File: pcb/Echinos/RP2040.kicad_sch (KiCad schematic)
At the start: 29 parts, among them J9 TagConnect_6pins, SW2 SW_Push, SW3 SW_Push, U4 W25Q128JVS, U5 RP2040, U6 74LVC1T45, X1 CMOS -12MHz

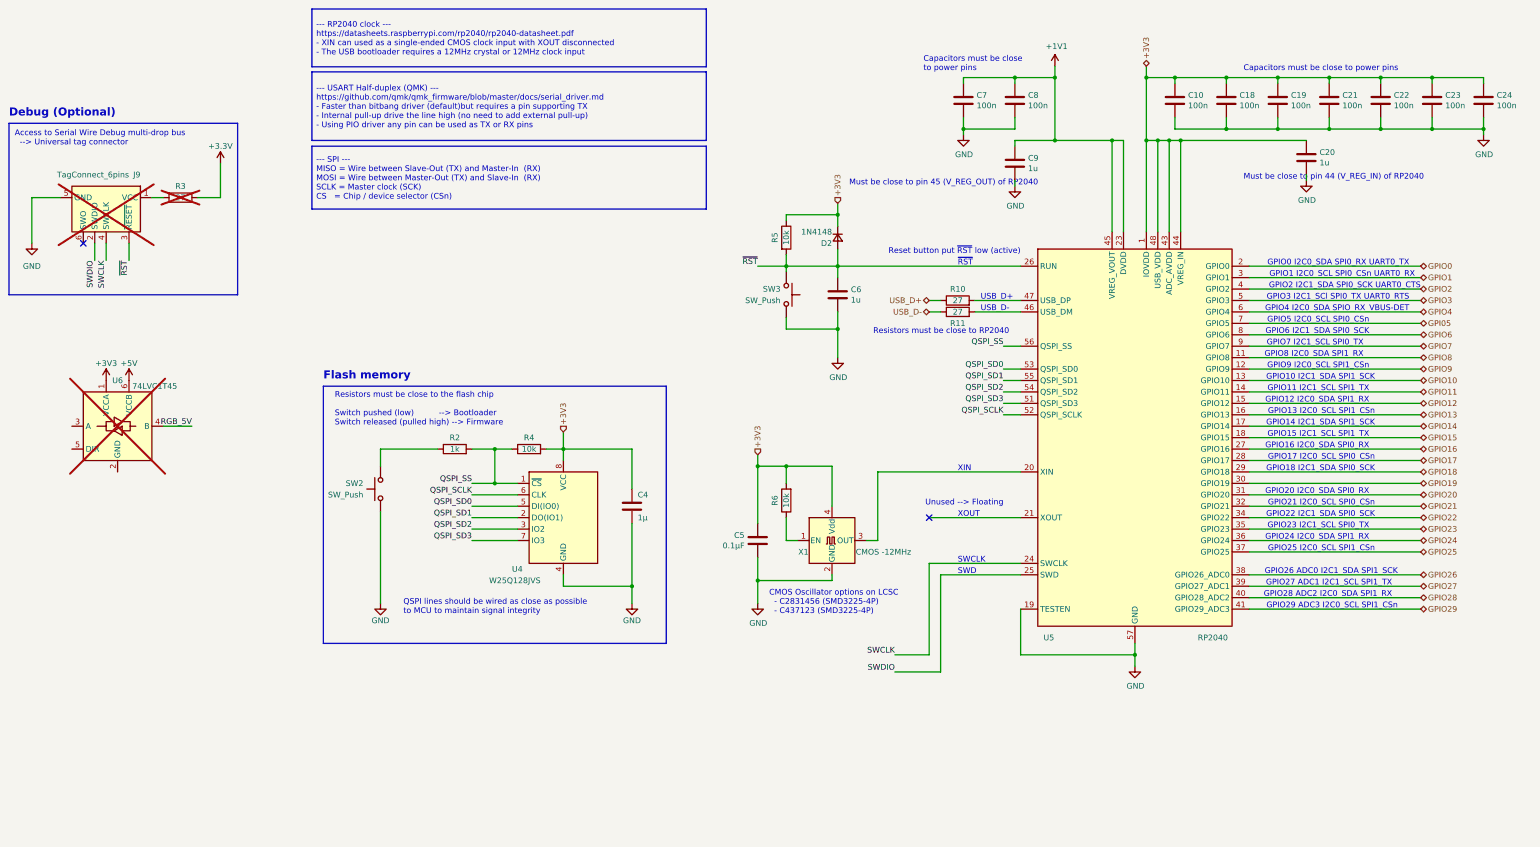
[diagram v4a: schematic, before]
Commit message: [PCB] - Save last state with on board RP2040.
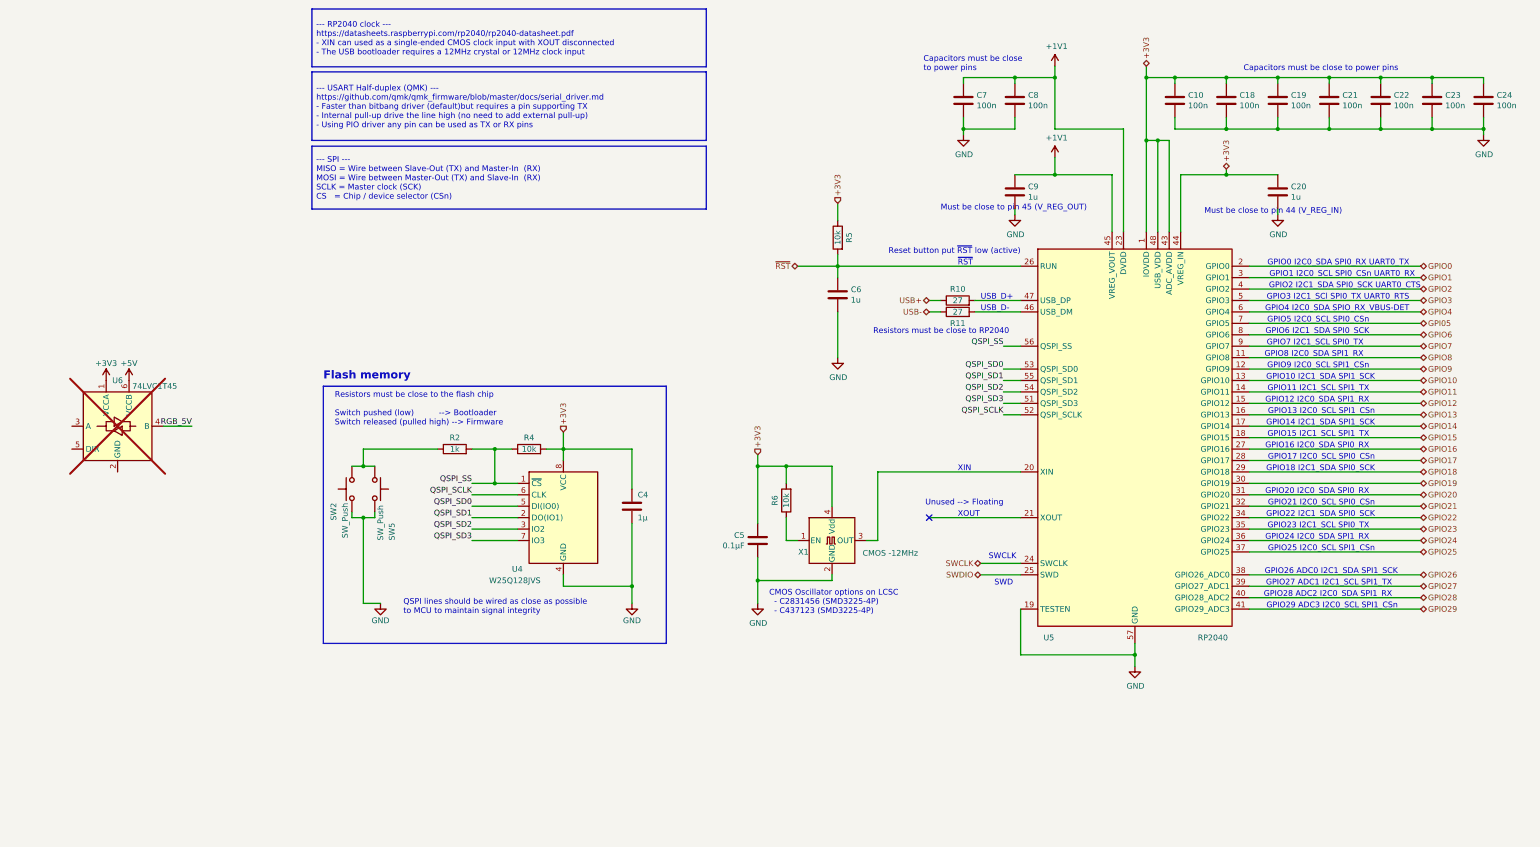
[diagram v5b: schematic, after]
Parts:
- removed D2: 1N4148, Diode_SMD:D_SOD-323_HandSoldering, symbol Device:D_Small
- removed J9: TagConnect_6pins, Connector:Tag-Connect_TC2030-IDC-FP_2x03_P1.27mm_Vertical, symbol Connector:Conn_ARM_SWD_TagConnect_TC2030
- removed R3: 27, Resistor_SMD:R_0402_1005Metric_Pad0.72x0.64mm_HandSolder, symbol Device:R
- removed SW3: SW_Push, Button_Switch_SMD:SW_SPST_CK_KXT3, symbol Switch:SW_Push
- added SW5: SW_Push, Button_Switch_SMD:SW_SPST_TS-1088-xR020, symbol Switch:SW_Push
- SW2: footprint Button_Switch_SMD:SW_SPST_CK_KXT3 -> Button_Switch_SMD:SW_SPST_TS-1088-xR020
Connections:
- net GND: now also SW5.2
- net at R2.1, SW2.2: now also SW5.1
- net USB_D+ renamed USB+
- net USB_D- renamed USB-
- no-connect marks 2 -> 1
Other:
- note added: "Must be close to pin 44 (V_REG_IN)"
- note added: "Must be close to pin 45 (V_REG_OUT)"
- note removed: "Access to Serial Wire Debug multi-drop bus --> Universal tag connector"
- note removed: "Debug (Optional)"
- note removed: "Must be close to pin 44 (V_REG_IN) of RP2040"
- note removed: "Must be close to pin 45 (V_REG_OUT) of RP2040"
- moved on the sheet: C20, C9, R5, SW2

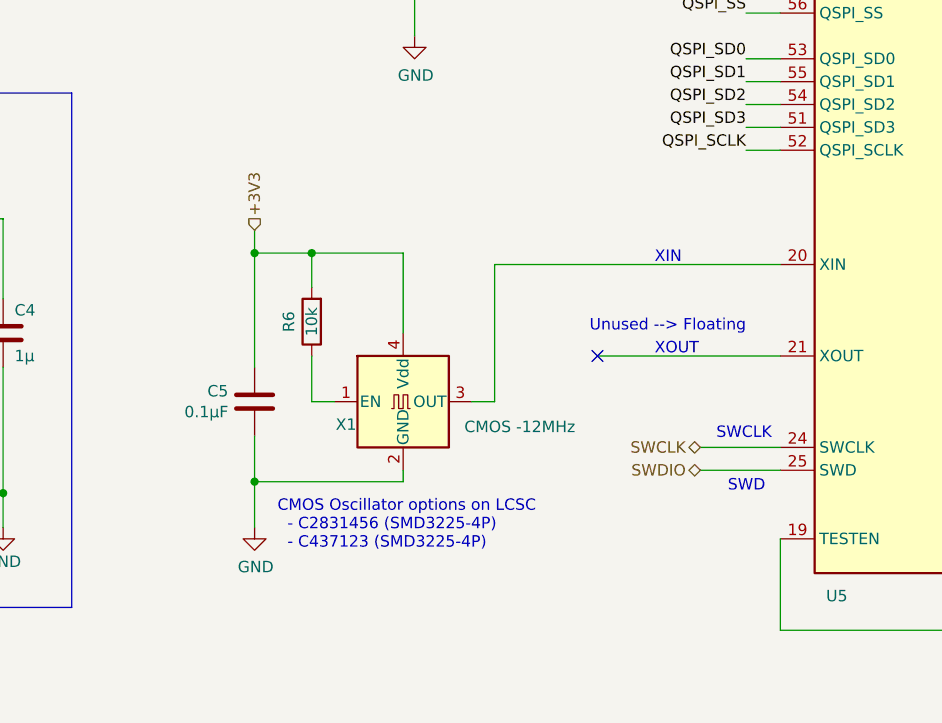
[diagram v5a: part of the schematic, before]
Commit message: [PCB] - Save last state with on board RP2040.   - Route crystal and 1V1
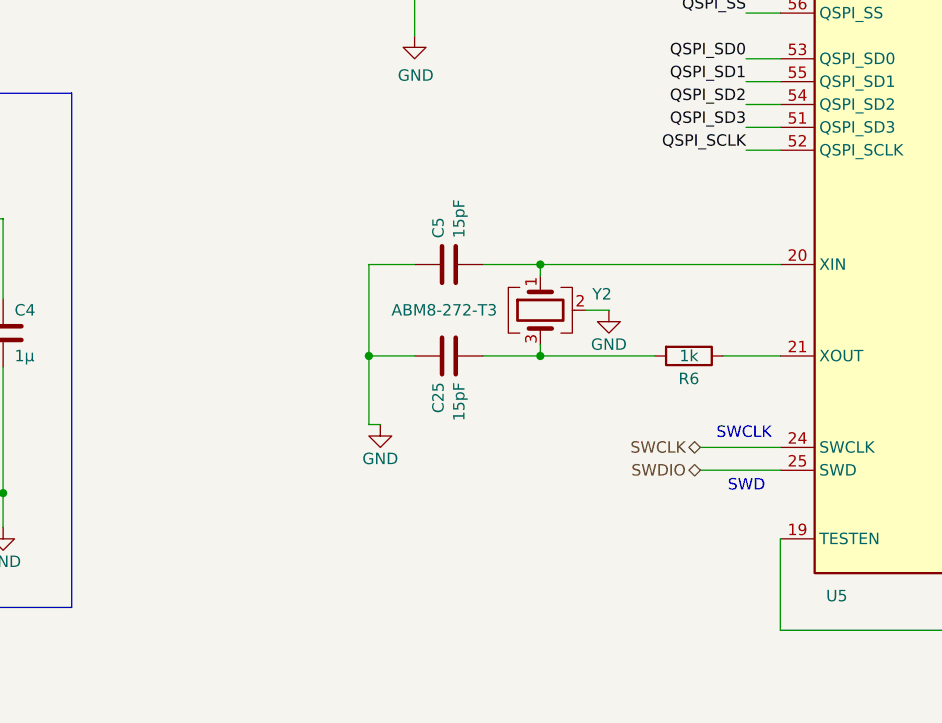
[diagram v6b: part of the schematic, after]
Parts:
- removed X1: CMOS -12MHz, Oscillator:Oscillator_SMD_Abracon_ASE-4Pin_3.2x2.5mm_HandSoldering, symbol Oscillator:ASE-xxxMHz
- added C25: 15pF, Capacitor_SMD:C_0402_1005Metric_Pad0.74x0.62mm_HandSolder, symbol Device:C
- added Y2: Crystal_GND24, Crystal:Crystal_SMD_Abracon_ABM8G-4Pin_3.2x2.5mm, symbol Device:Crystal_GND24
- C5: value 0.1µF -> 15pF; LCSC C5139511 -> C86285
- R6: value 10k -> 1k; LCSC C25744 -> C11702
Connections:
- net +3V3: no longer C5.1, R6.2
- net GND: now also C5.1, C25.1, Y2.2 (G), Y2.4 (G); no longer C5.2
- net at R6.1: now also U5.21 (XOUT)
- net at U5.20 (XIN): now also C5.2, Y2.1
- new net: C25.2, R6.2, Y2.3
- no-connect marks 1 -> 0
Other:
- note removed: "CMOS Oscillator options on LCSC - C2831456 (SMD3225-4P) - C437123 (SMD3225-4P)"
- note removed: "Unused --> Floating"
- note removed: "XIN"
- note removed: "XOUT"
- moved on the sheet: C5, R6

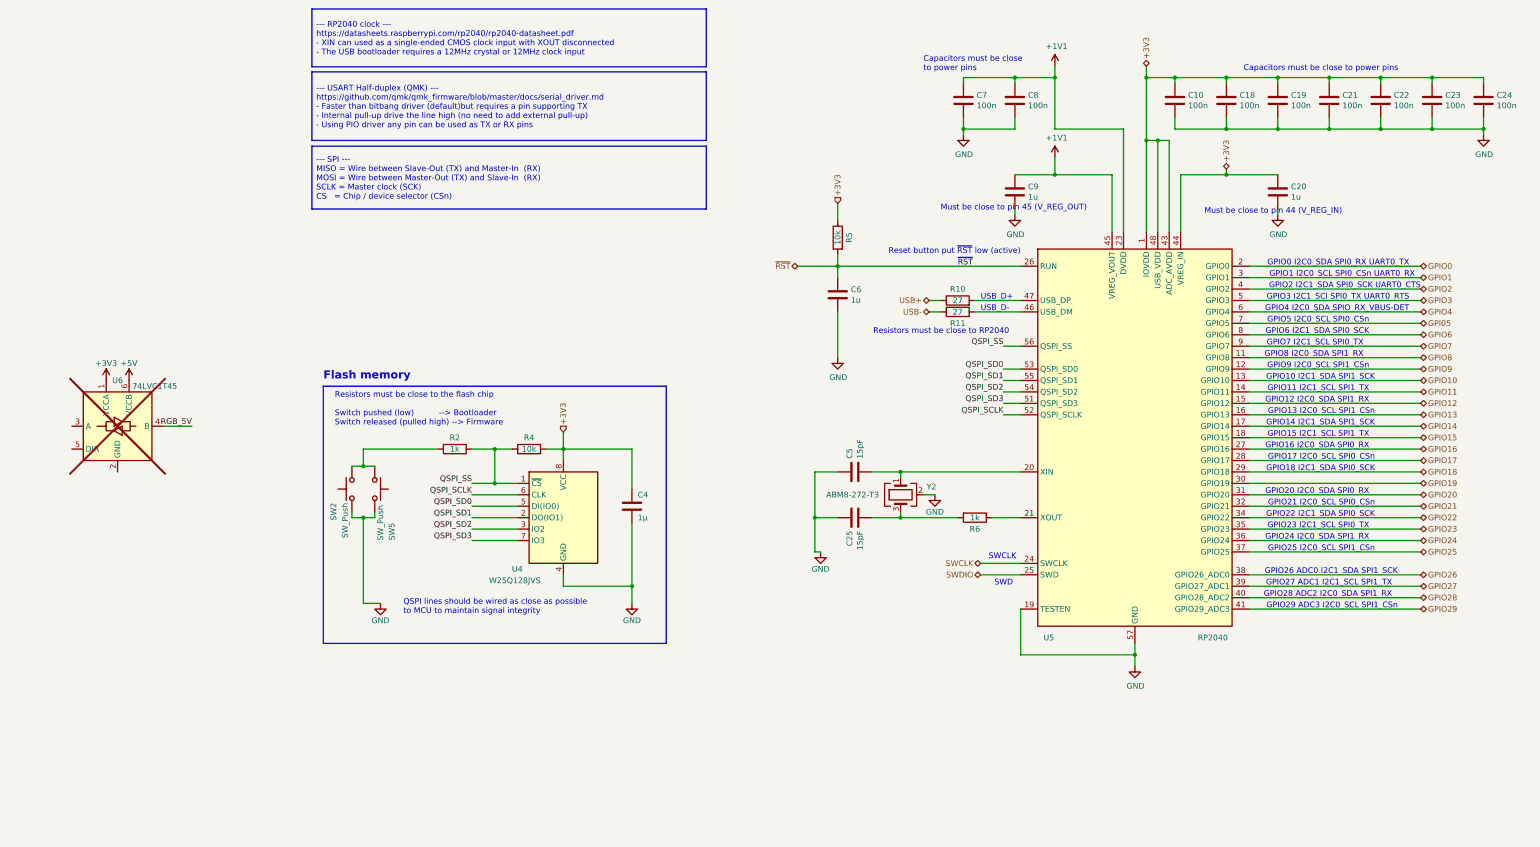
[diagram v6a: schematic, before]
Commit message: [PCB] - Save last state with on board RP2040.   - Clean schematics   - Fix flash capacitor value   - Fix flash schema to match all footprint pins   - Pass ERC (schema and pcb)   - Select missing LCSC components (USBC/B, buttons, vik connector)   - Add more margin to lateral pads in USB B footprint   - Improve top plane grounding under switches   - Adjust orientation and position to match JLCPCB   - Clean unused fields in schematics   - Add VIK connector footprint to lib (updated to match more models)   - Harmonization of footprints packaging for caps and resistors (either 0805 or 0402)   - Check availability and correctness of all parts   - Fix space in fields (was LCSC2 on leds)
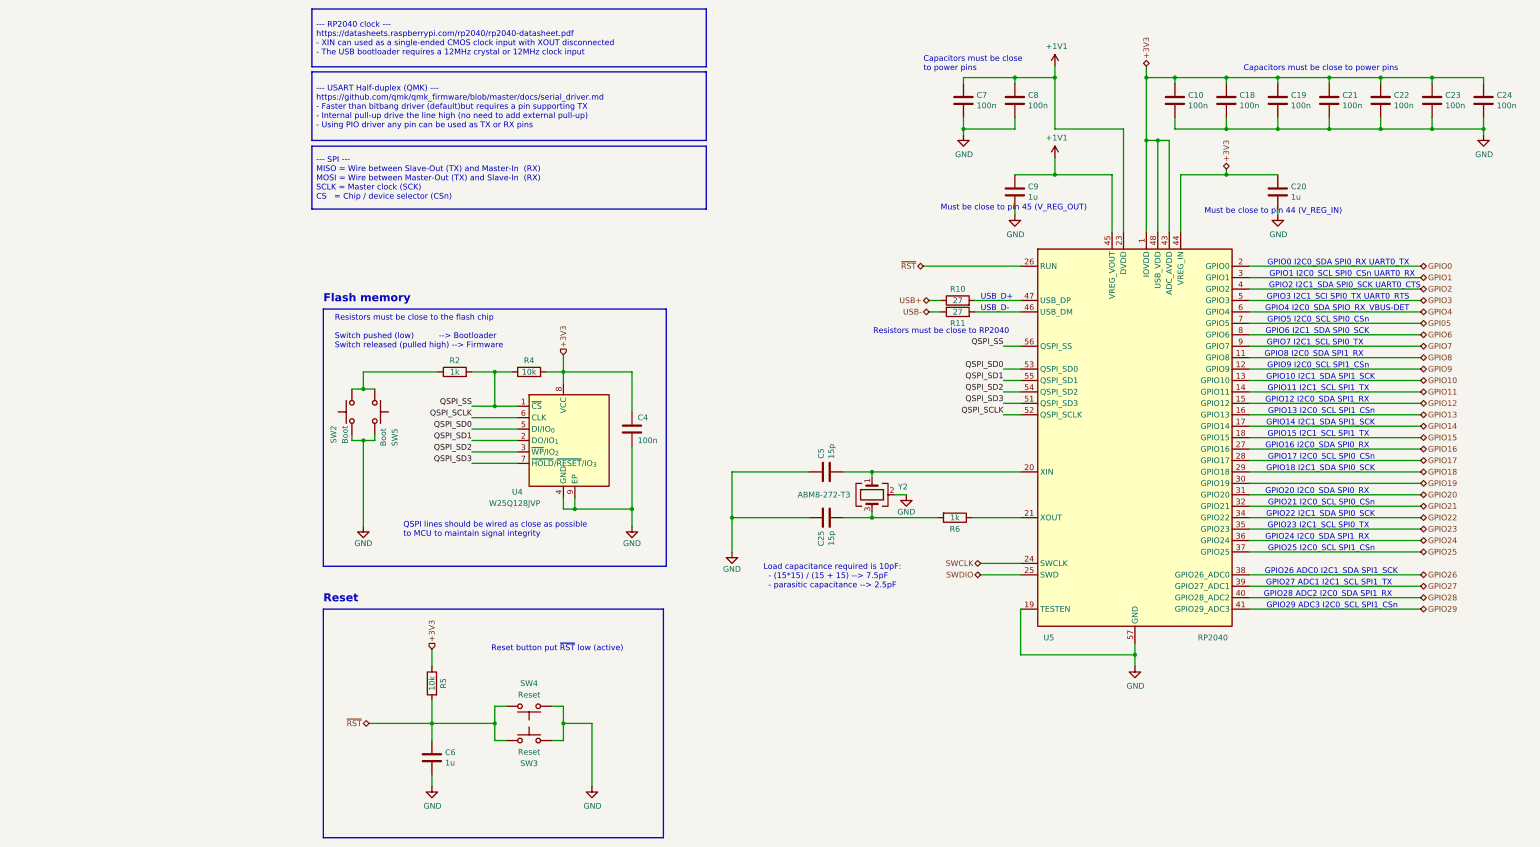
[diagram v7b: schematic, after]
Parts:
- removed U6: 74LVC1T45, Package_TO_SOT_SMD:SOT-563, symbol Logic_LevelTranslator:SN74LVC1T45DRL
- added SW3, SW4: Reset, Button_Switch_SMD:SW_SPST_TS-1088-xR020, symbol Switch:SW_Push
- C20, C9: LCSC C458913 -> C14445
- C25, C5: value 15pF -> 15p
- C4: value 1µ -> 100n; footprint Capacitor_SMD:C_0603_1608Metric_Pad1.08x0.95mm_HandSolder -> Capacitor_SMD:C_0805_2012Metric; LCSC C19666 -> C1711
- C6: LCSC C19666 -> C14445
- SW2, SW5: value SW_Push -> Boot; LCSC C319433 -> C720477
- U4: value W25Q128JVS -> W25Q128JVP; symbol Memory_Flash:W25Q128JVS -> Memory_Flash:W25Q128JVP; MPN (none) -> W25Q128JVPIQ
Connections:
- net GND: now also U4.9 (EP), SW3.2, SW4.1
- net ~{RST}: now also SW3.1, SW4.2
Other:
- note added: "Load capacitance required is 10pF: - (15*15) / (15 + 15) --> 7.5pF - parasitic capacitance --> 2.5pF"
- note added: "Reset"
- note removed: "SWCLK"
- note removed: "SWD"
- note removed: "~{RST}"
- moved on the sheet: C25, C4, C5, C6, R2, R4, R5, R6, SW2, SW5, Y2

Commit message: [PCB] - Save last state with on board RP2040.   - Create right side and route all components   - Component still on the bottom side to be able to merge both side for manufacturing
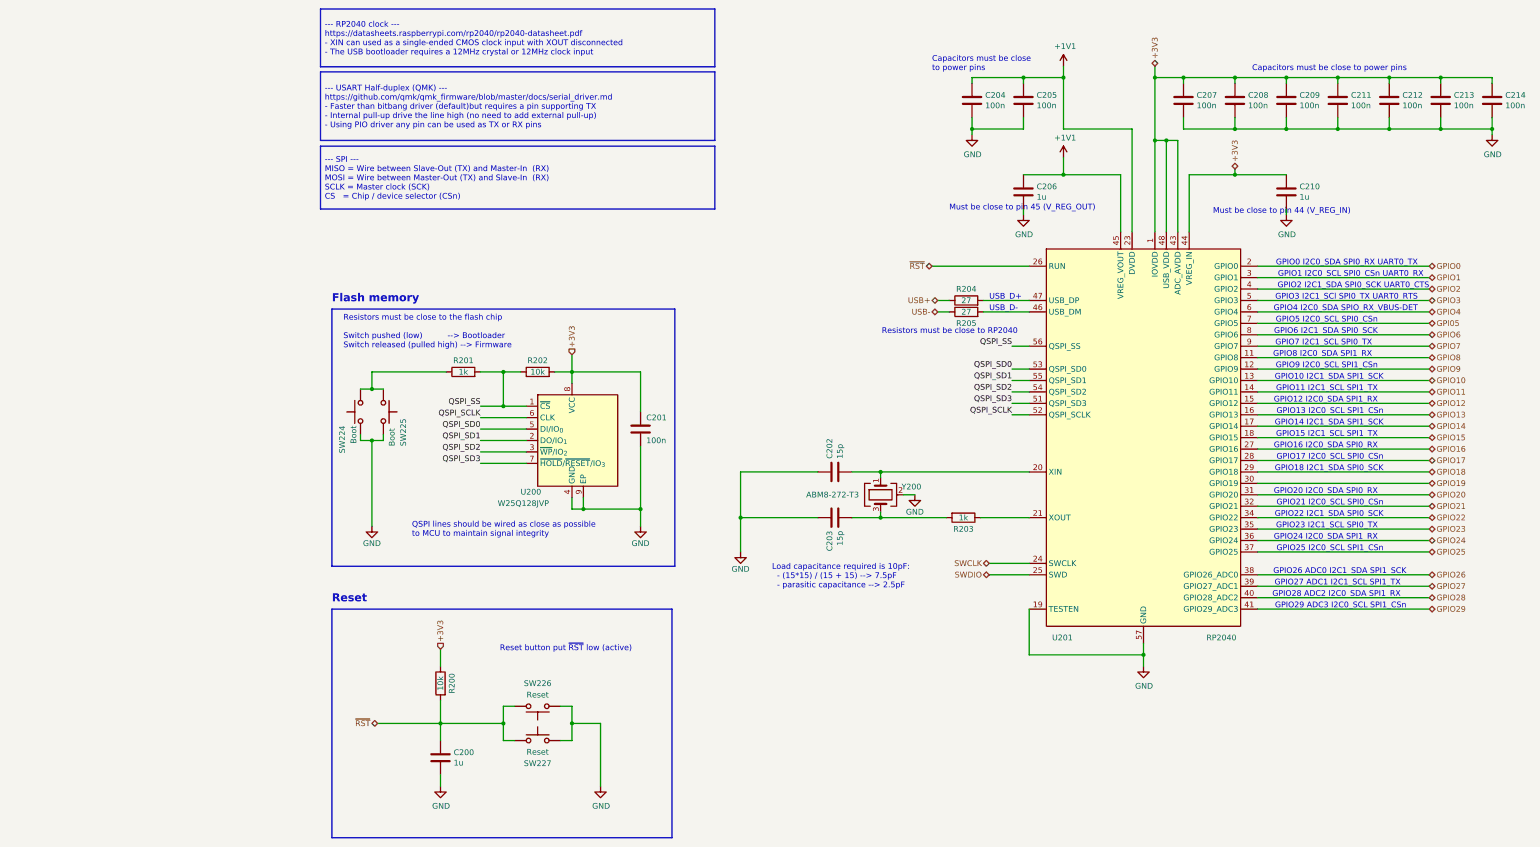
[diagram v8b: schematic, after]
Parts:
- renumbered C6 to C200, C4 to C201, C5 to C202, C25 to C203, C7 to C204, C8 to C205, C9 to C206, C10 to C207, C18 to C208, C19 to C209, C20 to C210, C21 to C211, C22 to C212, C23 to C213, C24 to C214, R5 to R200, R2 to R201, R4 to R202, R6 to R203, R10 to R204, R11 to R205, SW2 to SW224, SW5 to SW225, SW4 to SW226, SW3 to SW227, U4 to U200, U5 to U201, Y2 to Y200
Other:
- title: RP2040 -> RP2040 (Left)
- moved on the sheet: C200, C201, C202, C203, C204, C205, C206, C207, C208, C209, C210, C211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
